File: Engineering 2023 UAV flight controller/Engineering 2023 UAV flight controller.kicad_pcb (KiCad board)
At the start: 2 copper layers, 82 parts, among them J1 Micro_SD_Card, J2 ESC speed control, J3 USB_C_Receptacle_USB2.0, J4 Conn_Coaxial, J5 external power rail, J6 Board GPIO and the Lora DIO, J7 external ground rail, M1 Aileron Left, M2 Aileron Right, M3 Elevator Left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

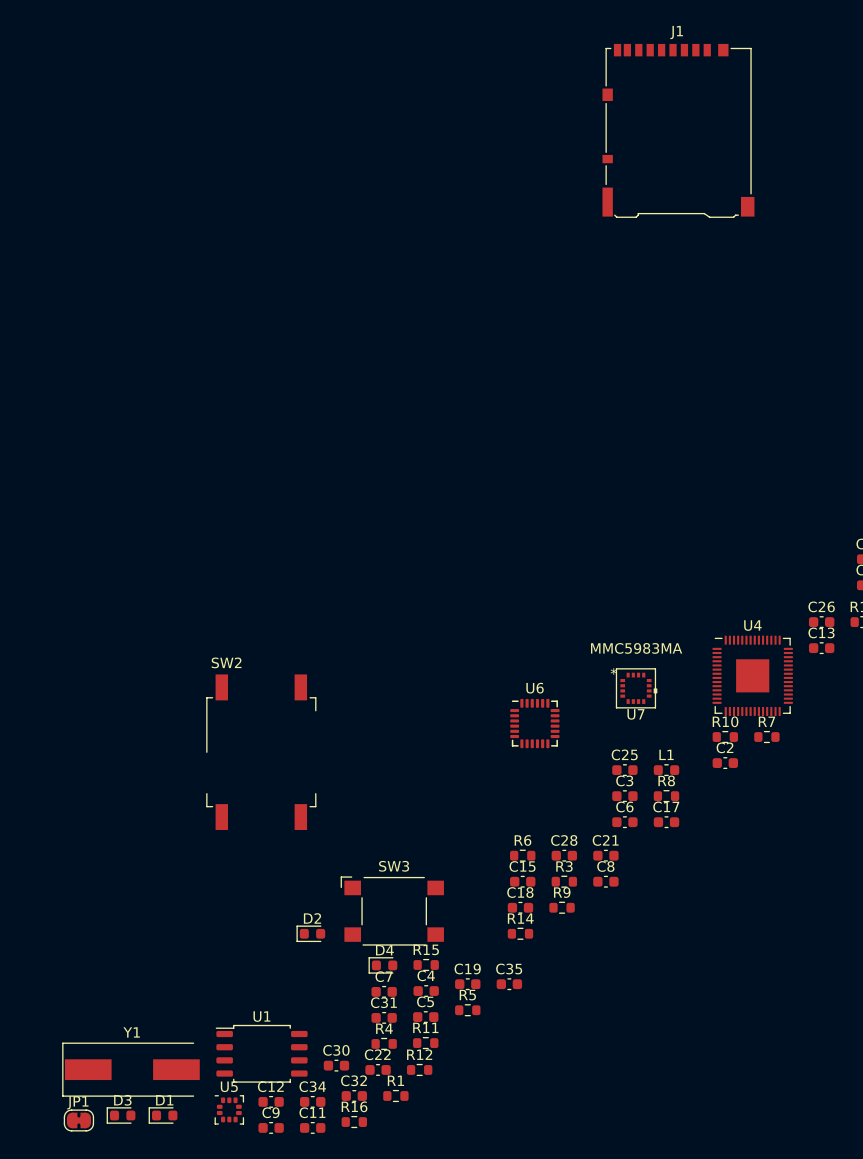
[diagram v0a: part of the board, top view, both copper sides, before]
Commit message: fixed some 3d shapes
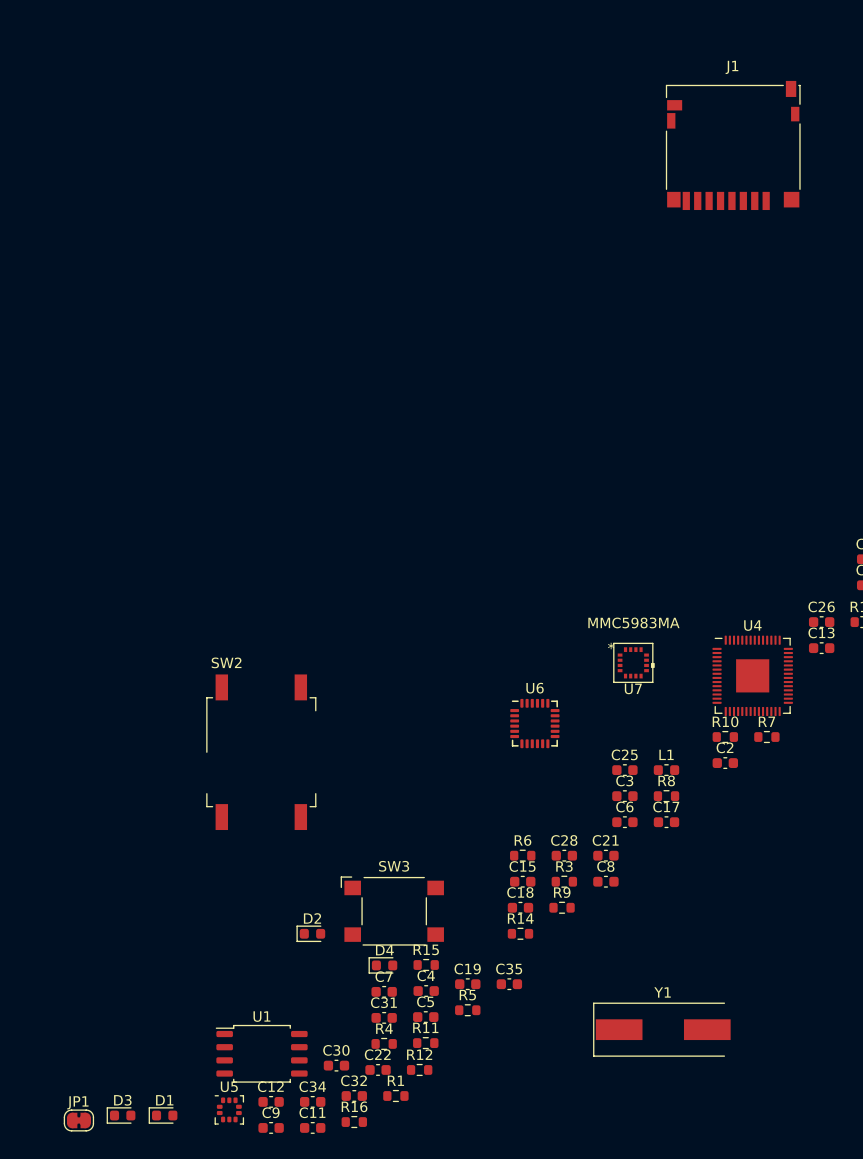
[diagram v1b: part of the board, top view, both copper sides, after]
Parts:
- J1: footprint Connector_Card:microSD_HC_Hirose_DM3AT-SF-PEJM5 -> Connector_Card:microSD_HC_Hirose_DM3D-SF
- moved Y1 51.3 mm to (199.5, 118.2)
- moved J1 5.48 mm to (206.2, 33.0)
- moved U7 2.47 mm to (196.6, 82.9)
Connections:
- net /USB_DM renamed /USB_D_N
- net /USB_DP renamed /USB_D_P
- net Net-(C25-Pad2) renamed /IMU_decouple_cap
- net Net-(C33-Pad2) renamed /MMC_CAP
- net Net-(C35-Pad1) renamed /phantom power
- net Net-(D4-Pad2) renamed /NEO_TIMEPULSE
- net Net-(J3-PadA5) renamed /CC1
- net Net-(J3-PadB5) renamed /CC2

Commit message: started component placement, finished placeing power?
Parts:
- added R18: 2k7, Resistor_SMD:R_0603_1608Metric, F.Cu at (107.0, 187.0)
- added R19: 2k7, Resistor_SMD:R_0603_1608Metric, F.Cu at (111.0, 187.0)
- R2: footprint Resistor_SMD:R_0603_1608Metric -> Potentiometer_SMD:Potentiometer_Bourns_3314R-GM5_Vertical
- moved C24 212.5 mm to (53.2, 194.0)
- moved C33 209.7 mm to (32.8, 171.0)
- moved R13 209.1 mm to (51.2, 174.0)
- moved C27 207.1 mm to (42.8, 181.0)
- moved U7 191.0 mm to (34.0, 183.0)
- moved C25 180.9 mm to (43.0, 190.0)
- moved R14 177.8 mm to (26.0, 187.0)
- moved R2 171.2 mm to (53.0, 90.0), turned to 180 degrees
- moved R15 166.6 mm to (25.0, 181.0)
- moved C1 166.0 mm to (63.0, 104.0), turned to 180 degrees
- moved R10 165.2 mm to (41.0, 105.0), turned to -90 degrees
- moved U6 163.4 mm to (53.0, 182.0)
- moved C2 158.9 mm to (47.0, 104.0), turned to 180 degrees
- moved C22 152.0 mm to (37.0, 192.0)
- moved C34 147.0 mm to (27.0, 174.0)
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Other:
- board outline added: 63 x 85 mm
- copper layers 2 -> 4
- board text added: "noise zone"

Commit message: some more component placement
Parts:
- moved R7 182.9 mm to (99.5, 106.8), turned to -90 degrees
- moved D1 180.0 mm to (99.5, 103.2), turned to 90 degrees
- moved R4 176.0 mm to (93.8, 97.2), turned to -90 degrees
- moved R3 174.3 mm to (88.2, 97.2), turned to -90 degrees
- moved J3 172.6 mm to (91.5, 105.5)
- moved R8 170.6 mm to (65.5, 64.8), turned to 90 degrees
- moved R9 168.1 mm to (64.0, 64.8), turned to 90 degrees
- moved C8 163.5 mm to (70.2, 38.2), turned to -90 degrees
- moved Y1 163.0 mm to (65.8, 43.8), turned to 180 degrees
- moved U4 161.6 mm to (65.5, 57.0), turned to 180 degrees
- moved C9 141.2 mm to (61.5, 38.2), turned to -90 degrees
- moved U1 129.4 mm to (74.8, 64.2)
- moved C12 119.4 mm to (114.5, 31.0)
- moved C7 119.4 mm to (105.6, 28.0)
- moved C11 119.4 mm to (118.5, 33.5)
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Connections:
- U1 pad 6: /QSPI_SS -> /QSPI_SCLK
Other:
- board size 63 x 85 mm -> 70 x 85 mm

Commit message: finished first layout itteration
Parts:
- added C36: 1u, Capacitor_SMD:C_0603_1608Metric, F.Cu at (182.2, 84.0)
- moved R15 181.8 mm to (174.0, 76.8)
- moved C22 181.2 mm to (170.7, 69.8), turned to -90 degrees
- moved R14 180.1 mm to (170.7, 79.8), turned to -90 degrees
- moved U7 179.7 mm to (181.5, 80.3), turned to 90 degrees
- moved C34 177.8 mm to (177.5, 79.3)
- moved C25 176.4 mm to (175.7, 73.8), turned to 180 degrees
- moved C33 176.4 mm to (181.7, 76.5), turned to -90 degrees
- moved C24 170.6 mm to (175.7, 75.3), turned to 180 degrees
- moved C27 162.6 mm to (165.0, 73.8)
- moved U6 158.5 mm to (169.5, 74.5), turned to 90 degrees
- moved R12 154.0 mm to (162.0, 76.8), turned to 180 degrees
- moved R13 148.4 mm to (162.0, 75.3), turned to 180 degrees
- moved SW3 144.8 mm to (124.2, 37.2)
- moved C31 144.7 mm to (126.8, 56.9), turned to -90 degrees
- moved C30 139.4 mm to (125.2, 56.9), turned to -90 degrees
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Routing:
- net /USB_D_N: track 0.00 -> 54.3 mm
- net /USB_D_P: track 0.00 -> 51.4 mm
- added copper zone on In2.Cu, net /3.3v rail
- added copper zone on B.Cu, net GND
- added copper zone on F.Cu, net GND
- added copper zone on In1.Cu, net GND
- added copper zone on In2.Cu, net GND
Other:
- board size 70 x 85 mm -> 70 x 120 mm
- board text added: "no reason to put anything here"
- board text added: "second noise zone"

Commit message: started routing
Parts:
- added C37: 100n, Capacitor_SMD:C_0603_1608Metric, F.Cu at (152.0, 117.0)
- J2, M1, M2, M3, M4: footprint Connector_PinSocket_2.54mm:PinSocket_1x03_P2.54mm_Vertical -> Connector_PinHeader_2.54mm:PinHeader_1x03_P2.54mm_Vertical
- J6: footprint Connector_PinSocket_2.54mm:PinSocket_1x13_P2.54mm_Vertical -> Connector_PinHeader_2.54mm:PinHeader_1x13_P2.54mm_Vertical
- moved C11 1.78 mm to (146.5, 99.2)
- moved C19 1.78 mm to (148.0, 99.2)
- moved C10 1.58 mm to (155.0, 117.0)
- moved C13 1.58 mm to (153.5, 117.0)
- moved C15 1.48 mm to (141.8, 109.8)
- moved C17 1.29 mm to (157.8, 110.2)
- moved C18 1.28 mm to (157.8, 106.3)
- moved C16 1.22 mm to (142.0, 106.3)
- moved R6 1.15 mm to (167.2, 111.0)
- moved R18 1.00 mm to (161.2, 103.0), turned to 0 degrees
- moved C12 1.00 mm to (145.7, 114.5)
- moved C1 0.32 mm to (147.5, 147.1)
- moved C8 0.22 mm to (154.5, 89.3)
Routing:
- net /USB_C positive rail: track 0.00 -> 99.6 mm
- net /Servo 6V rail: track 0.00 -> 95.5 mm
- net /3.3v rail: track 0.00 -> 93.9 mm, vias 0 -> 20
- net /reg in: track 0.00 -> 50.1 mm, vias 0 -> 1
- net GND: track 0.00 -> 42.0 mm, vias 0 -> 84
- net /External_pin_4: track 0.00 -> 37.1 mm
- net /External_pin_5: track 0.00 -> 34.2 mm
- net /External_pin_6: track 0.00 -> 31.8 mm
- net /External_pin_7: track 0.00 -> 29.4 mm
- net /External_pin_8: track 0.00 -> 27.5 mm
- net /Elevator Right PWM: track 0.00 -> 26.9 mm
- net /External_pin_9: track 0.00 -> 26.0 mm
- net /Elevator Left PWM: track 0.00 -> 25.6 mm
- net /QSPI_SS: track 0.00 -> 24.5 mm
- net /Aileron Right PWM: track 0.00 -> 24.2 mm
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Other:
- board text added: "+"
- board text added: "-"
- board text added: "DIO 1"
- board text added: "GPIO 1"

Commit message: pcb revision one completed, the png's are for the reddit gods to review.
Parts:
- added H1: MountingHole, MountingHole:MountingHole_3.2mm_M3, F.Cu at (148.8, 76.0)
- added H2: MountingHole, MountingHole:MountingHole_3.2mm_M3, F.Cu at (119.8, 62.2)
- added H3: MountingHole, MountingHole:MountingHole_3.2mm_M3, F.Cu at (180.8, 124.2)
- added J10: DIO, Connector_PinHeader_2.54mm:PinHeader_1x03_P2.54mm_Vertical, F.Cu at (152.4, 51.1)
- added J8: Serial wire debug, Connector_PinHeader_2.54mm:PinHeader_1x02_P2.54mm_Vertical, F.Cu at (136.5, 88.0)
- added J9: reset short?, Connector_PinHeader_2.54mm:PinHeader_1x02_P2.54mm_Vertical, F.Cu at (136.5, 82.0)
- J6: value Board GPIO and the Lora DIO -> GPIO; footprint Connector_PinHeader_2.54mm:PinHeader_1x13_P2.54mm_Vertical -> Connector_PinHeader_2.54mm:PinHeader_1x10_P2.54mm_Vertical
- moved R12 22.4 mm to (169.2, 98.0), turned to 0 degrees
- moved C35 22.0 mm to (160.8, 52.6), turned to 180 degrees
- moved R13 21.7 mm to (166.0, 96.6)
- moved J4 19.3 mm to (163.2, 46.2), turned to 0 degrees
- moved L1 17.4 mm to (163.2, 51.8), turned to 90 degrees
- moved C32 16.7 mm to (184.6, 88.2), turned to 90 degrees
- moved C27 16.0 mm to (165.5, 89.8), turned to 90 degrees
- moved C22 15.5 mm to (162.0, 82.6), turned to 0 degrees
- moved C33 13.9 mm to (168.2, 73.0), turned to 0 degrees
- moved C36 13.9 mm to (175.7, 71.7), turned to -90 degrees
- moved R17 13.8 mm to (165.8, 52.6), turned to 180 degrees
- moved C25 12.7 mm to (164.2, 79.2), turned to -90 degrees
- moved U7 11.8 mm to (172.0, 73.2), turned to 180 degrees
- moved U6 11.2 mm to (166.2, 85.2), turned to 180 degrees
- moved SW3 10.7 mm to (122.0, 47.6)
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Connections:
- C25 pad 2: /IMU_decouple_cap -> /IMU_REGOUT
- C27 pad 2: /IMU_decouple_cap -> /IMU_CPOUT
- U6 pad 10: /IMU_decouple_cap -> /IMU_REGOUT
- U6 pad 20: /IMU_decouple_cap -> /IMU_CPOUT
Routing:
- net /LORA_TX_EN: track 1.73 -> 122.5 mm, vias 1 -> 2
- net /NEO_RXD: track 1.23 -> 94.0 mm, vias 1 -> 2
- net /NEO_TXD: track 1.25 -> 93.6 mm, vias 1 -> 2
- net /LORA_RX_EN: track 1.47 -> 93.5 mm, vias 1 -> 2
- net /LORA_MISO: track 0.00 -> 82.3 mm, vias 0 -> 2
- net /LORA_~{SS}: track 0.00 -> 82.1 mm
- net /LORA SCK: track 0.00 -> 80.0 mm
- net /LORA_BUSY: track 0.00 -> 78.1 mm, vias 0 -> 2
- net /LORA_MOSI: track 0.00 -> 77.4 mm
- net /External_pin_1: track 1.63 -> 56.6 mm, vias 1 -> 2
- net /External_pin_2: track 1.18 -> 53.6 mm, vias 1 -> 2
- net /External_pin_3: track 1.62 -> 52.3 mm, vias 1 -> 2
- net /3.3v rail: track 93.9 -> 135.7 mm, vias 20 -> 34
- net /microSD_CS: track 2.79 -> 43.1 mm
- net /microSD_CLK: track 2.76 -> 42.5 mm
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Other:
- board size 70 x 120 mm -> 70.1 x 100 mm
- board text added: "GND"
- board text added: "RUN"
- board text added: "SWCLK"
- board text added: "SWD"
- board text removed: "no reason to put anything here"
- board text removed: "noise zone"

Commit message: got some work to do
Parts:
- removed H1, H2, H3: MountingHole, MountingHole:MountingHole_3.2mm_M3
- C35: value 47p -> 10n
- J4: moved to B.Cu
- moved SW3 27.4 mm to (149.0, 52.0)
- moved C30 14.8 mm to (138.8, 63.0), turned to 180 degrees
- moved C31 14.3 mm to (138.8, 64.6), turned to 180 degrees
- moved U8 9.36 mm to (143.4, 52.3), turned to -90 degrees
- moved J10 4.88 mm to (152.3, 46.2), turned to -90 degrees
- moved C35 0.20 mm to (160.6, 52.6)
- turned J4 to 180 degrees
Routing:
- net /LORA_TX_EN: track 122.5 -> 91.9 mm
- net /LORA_RX_EN: track 93.5 -> 76.4 mm
- net /DIO1: track 8.01 -> 20.8 mm
- net /DIO2: track 7.82 -> 17.6 mm
- net /LORA_MISO: track 82.3 -> 74.8 mm
- net /LORA_MOSI: track 77.4 -> 70.0 mm
- net /LORA_~{RESET}: track 30.4 -> 23.2 mm
- net /LORA_BUSY: track 78.1 -> 85.0 mm
- net /LORA SCK: track 80.0 -> 74.4 mm
- net /3.3v rail: track 135.7 -> 131.1 mm
- net GND: track 67.6 -> 72.0 mm, vias 112 -> 101
- net /LORA_~{SS}: track 82.1 -> 78.0 mm
- net /DIO3: track 8.34 -> 10.6 mm
- net (no net): vias 2 -> 1
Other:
- board text added: "TODO: reroute pcb to add space at power zone for a switching regulator, add tabs for pcb mounting"

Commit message: even ore stuff been done, board has been space optimised
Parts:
- removed C1, C2, C4, C6: 0.1uf, Capacitor_SMD:C_0603_1608Metric
- removed C3, C5: 1uf, Capacitor_SMD:C_0603_1608Metric
- removed D2: LED_GREEN, LED_SMD:LED_0603_1608Metric
- removed D3: LED_RED, LED_SMD:LED_0603_1608Metric
- removed J2: ESC speed control, Connector_PinHeader_2.54mm:PinHeader_1x03_P2.54mm_Vertical
- removed R1: R, Resistor_SMD:R_0603_1608Metric
- removed R10, R11: 330, Resistor_SMD:R_0603_1608Metric
- removed R2: R_Trim, Potentiometer_SMD:Potentiometer_Bourns_3314R-GM5_Vertical
- removed SW1: SW_SPDT, Button_Switch_SMD:SW_SPDT_CK-JS102011SAQN
- removed U2: NCP1117-3.3_TO252, Package_TO_SOT_SMD:TO-252-2
- removed U3: LM350_TO220, Package_TO_SOT_THT:TO-220-3_Vertical
- moved J8 41.3 mm to (97.2, 100.6)
- moved J9 41.3 mm to (97.2, 94.6)
- moved R7 37.1 mm to (185.4, 102.6), turned to 0 degrees
- moved D1 33.4 mm to (181.9, 102.6), turned to 180 degrees
- moved J3 29.4 mm to (184.1, 110.6), turned to 90 degrees
- moved R4 21.7 mm to (175.9, 108.3), turned to 0 degrees
- moved R3 16.9 mm to (175.9, 113.8), turned to 0 degrees
- moved C27 16.6 mm to (168.8, 73.5), turned to 0 degrees
- moved C10 16.0 mm to (157.0, 101.1)
- moved C11 16.0 mm to (148.6, 83.3)
- moved C12 16.0 mm to (147.8, 98.6)
- moved C13 16.0 mm to (155.5, 101.1)
- moved C14 16.0 mm to (146.3, 97.6)
- moved C15 16.0 mm to (143.8, 93.8)
- moved C16 16.0 mm to (144.1, 90.4)
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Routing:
- net /Servo 6V rail: track 73.9 -> 11.0 mm, vias 1 -> 0
- net /USB_C positive rail: track 73.6 -> 21.9 mm
- net /reg in: track 50.9 -> 0.00 mm
- net /RUN: track 38.4 -> 5.06 mm
- net /SWCLK: track 29.3 -> 3.61 mm
- net /3.3v rail: track 131.1 -> 109.8 mm, vias 34 -> 27
- net /IMU_AUX_SCL: track 37.6 -> 16.6 mm
- net /ESC PWM: track 28.2 -> 9.05 mm
- net /SWD: track 24.8 -> 6.91 mm
- net /ESC positive rail: track 17.6 -> 0.00 mm
- net /LORA_BUSY: track 85.0 -> 68.4 mm
- net /LORA_RX_EN: track 76.4 -> 61.4 mm
- net /LORA_TX_EN: track 91.9 -> 77.2 mm
- net /LORA SCK: track 74.4 -> 61.0 mm
- net /LORA_MOSI: track 70.0 -> 56.9 mm
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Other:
- board size 70.1 x 100 mm -> 72.7 x 100 mm
